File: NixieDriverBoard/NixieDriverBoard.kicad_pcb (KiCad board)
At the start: 2 copper layers, 48.3 x 53.3 mm, 9 parts, among them K155ID1 K155ID1, K155ID2 K155ID1

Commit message: Updates nixie boards
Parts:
- 74HC595: renamed from 74HC1; footprint Housings_DIP:DIP-16_W7.62mm_LongPads -> BetterDIP:DIP-16_W7.62mm_LongPads_better
- K155ID1, K155ID2: footprint Housings_DIP:DIP-16_W7.62mm_LongPads -> BetterDIP:DIP-16_W7.62mm_LongPads_better
- renumbered R1 to 68K, R2 to 68K, CONN2 to ?, CONN1 to ?
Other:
- board text added: "+170V"
- board text added: "+5V"
- board text added: "1"
- board text added: "2"
- board text added: "3"
- board text added: "4"
- board text added: "5"
- board text added: "6"
- board text added: "CLK"
- board text added: "DATA"
- board text added: "GND"
- board text added: "PROP"

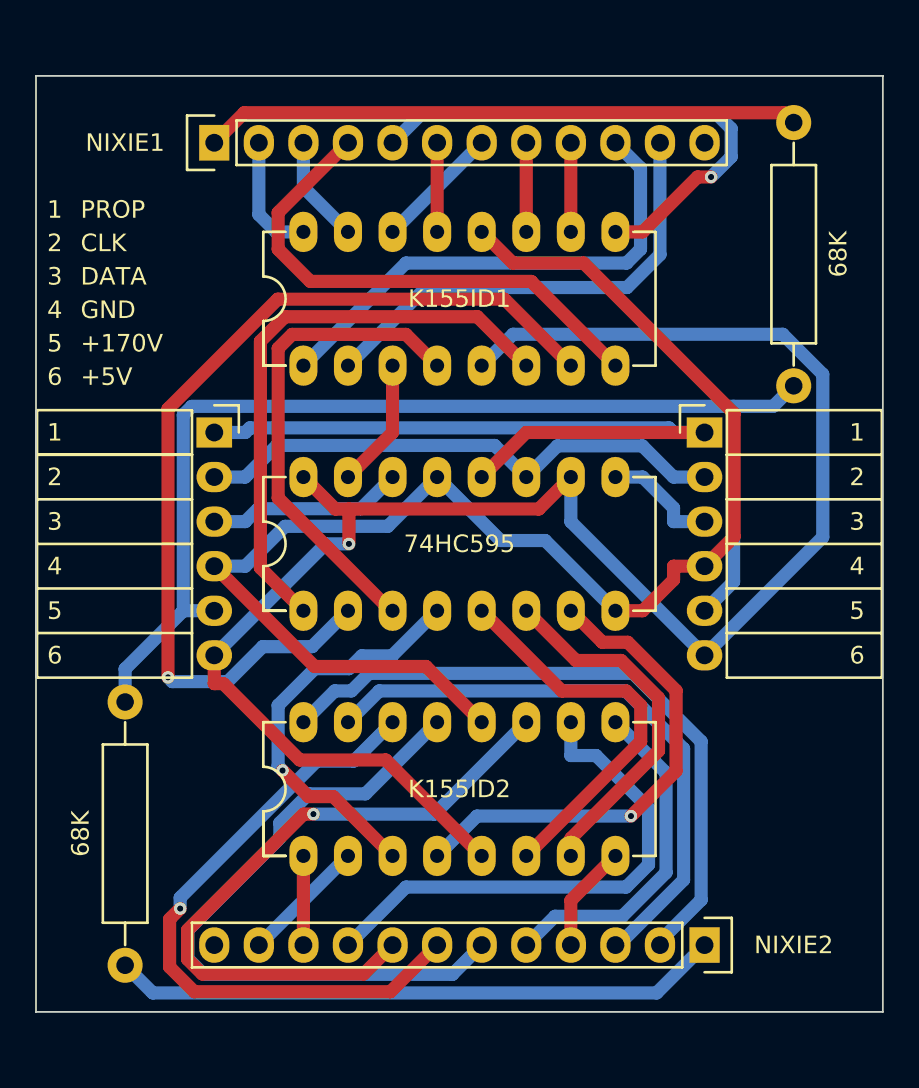
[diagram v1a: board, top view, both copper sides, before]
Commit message: Makes driver board more intuitive, and cleans up the silkscreen layers on both boards
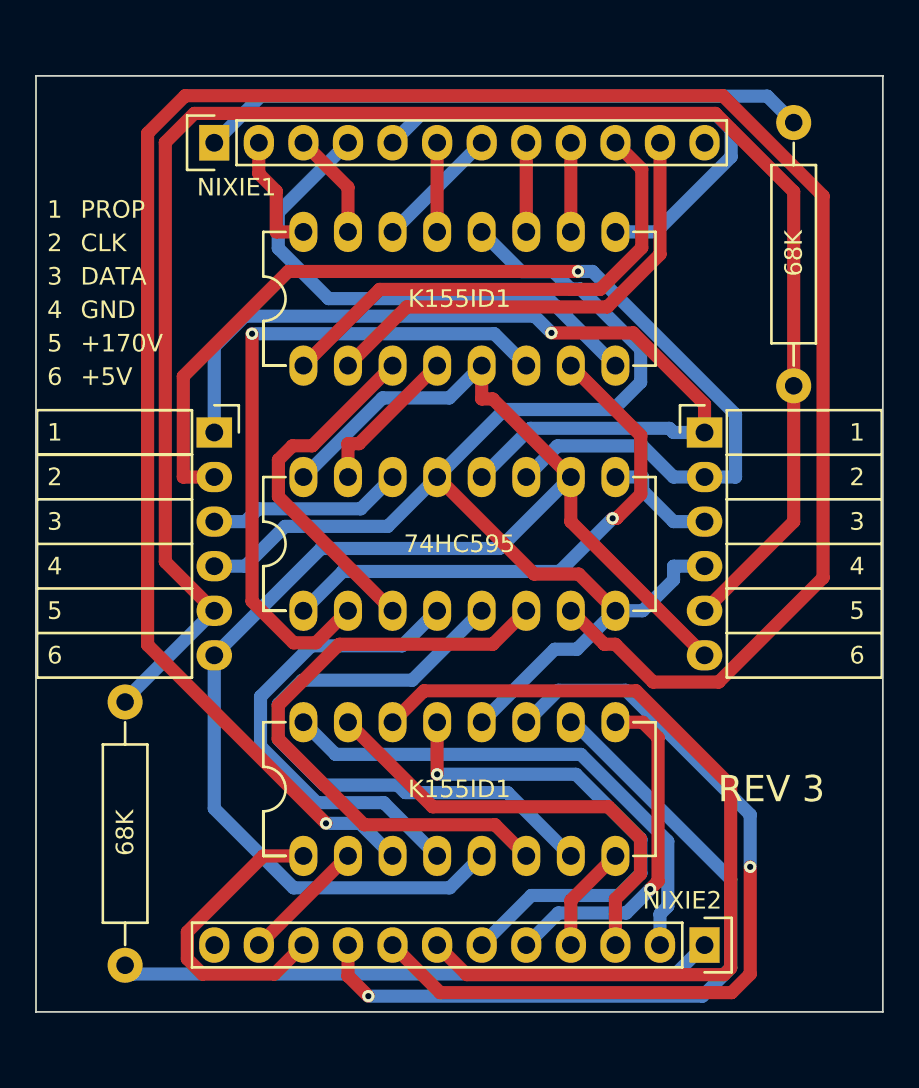
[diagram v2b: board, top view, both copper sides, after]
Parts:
- gave numbers to parts that had none: 2
- renumbered 74HC595 to 74HC1, 68K to R1, 68K to R2
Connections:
- K155ID1 pad 3: Net-(74HC1-Pad15) -> Net-(74HC1-Pad3)
- K155ID1 pad 4: Net-(74HC1-Pad3) -> Net-(74HC1-Pad15)
- K155ID1 pad 6: Net-(74HC1-Pad1) -> Net-(74HC1-Pad2)
- K155ID1 pad 7: Net-(74HC1-Pad2) -> Net-(74HC1-Pad1)
- K155ID2 pad 3: Net-(74HC1-Pad4) -> Net-(74HC1-Pad7)
- K155ID2 pad 4: Net-(74HC1-Pad7) -> Net-(74HC1-Pad4)
- K155ID2 pad 6: Net-(74HC1-Pad5) -> Net-(74HC1-Pad6)
- K155ID2 pad 7: Net-(74HC1-Pad6) -> Net-(74HC1-Pad5)
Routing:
- net Net-(74HC1-Pad7): track 28.1 -> 130.1 mm
- net VDD: track 67.3 -> 99.5 mm
- net /CLK: track 30.9 -> 61.8 mm, vias 0 -> 1
- net VCC: track 103.2 -> 86.1 mm, vias 1 -> 0
- net Net-(74HC1-Pad2): track 54.4 -> 38.8 mm
- net Net-(74HC1-Pad6): track 20.7 -> 35.2 mm
- net Net-(K155ID2-Pad14): track 37.4 -> 50.2 mm, vias 1 -> 0
- net Net-(K155ID2-Pad10): track 29.8 -> 42.6 mm, vias 0 -> 1
- net Net-(74HC1-Pad5): track 22.6 -> 35.2 mm
- net Net-(K155ID2-Pad1): track 5.08 -> 17.6 mm
- net Net-(K155ID2-Pad13): track 39.1 -> 28.8 mm, vias 0 -> 1
- net /PROP: track 41.9 -> 51.2 mm, vias 0 -> 1
- net GND: track 81.7 -> 72.5 mm
- net Net-(K155ID2-Pad11): track 38.6 -> 47.5 mm
- net Net-(K155ID2-Pad16): track 38.0 -> 29.7 mm
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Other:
- board text added: "68K"
- board text added: "74HC595"
- board text added: "K155ID1"
- board text added: "REV 3"
